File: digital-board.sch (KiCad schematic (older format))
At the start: 233 parts, among them IC1 ATMEGA6450-A, J1 CONN_20X2, Q1 2N3904, Q2 2N3904, SW15 TACT_SWITCH, SW16 TACT_SWITCH, SW17 TACT_SWITCH, SW18 TACT_SWITCH, SW19 TACT_SWITCH, SW20 TACT_SWITCH, SW21 TACT_SWITCH, SW22 TACT_SWITCH, SW23 TACT_SWITCH, U1 DG419, U10 74LVC1G32, U11 74HC165, U12 74AC595, U13 74AC595, U14 74HC165, U15 74AC595, U16 74AC595, U2 74HC4067, U3 R-78E5.0-1.0, U4 74HC4067, U5 74LS573, U6 74LS573, U7 74LVC2G04, U8 74AC595, U9 74HC165, X1 MIDI OUT, X2 MIDI IN, X3 MIDI THRU

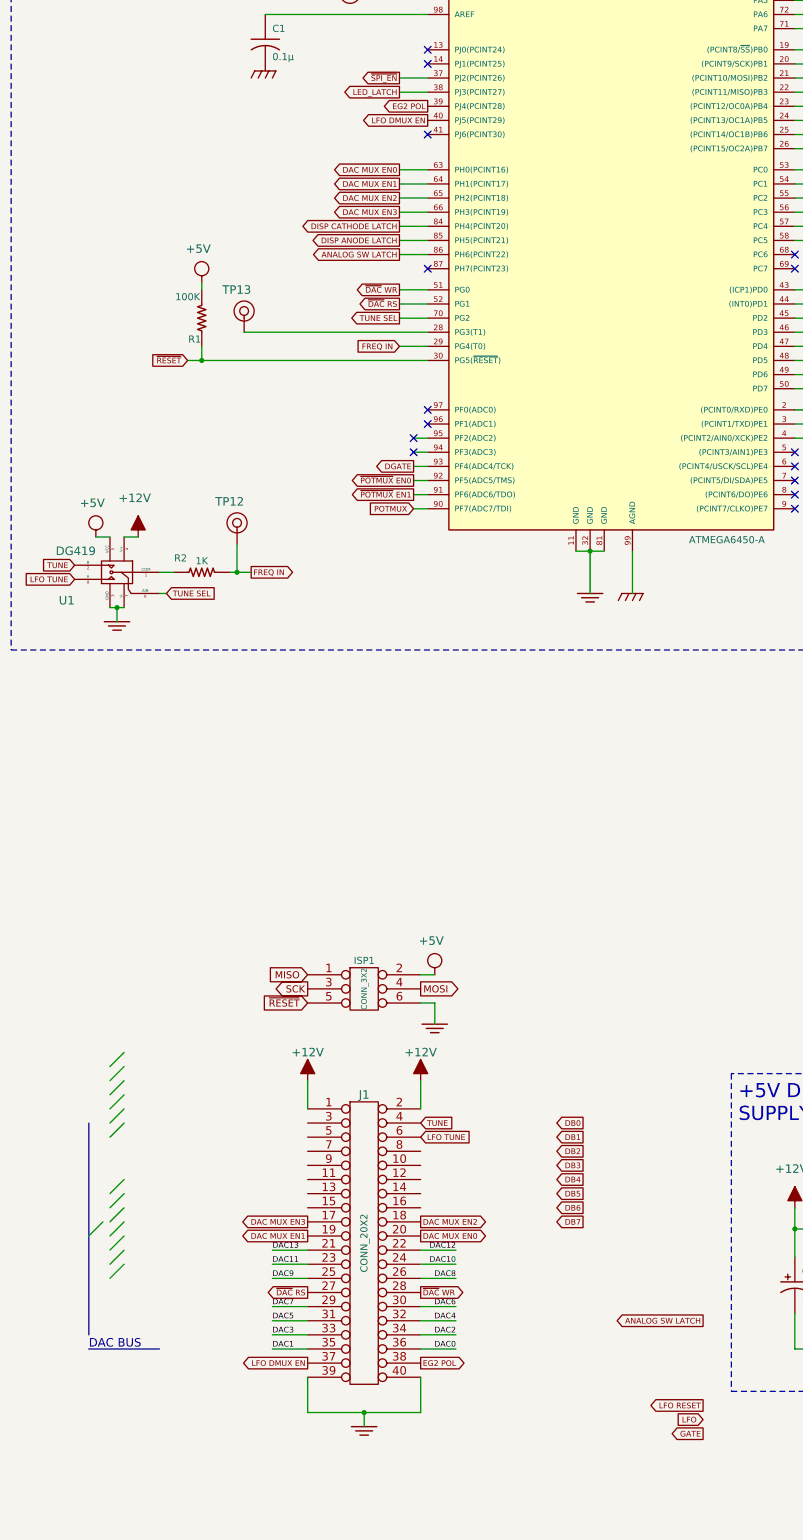
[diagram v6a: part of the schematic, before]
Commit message: almost done routing DAC and DATABUS to J1
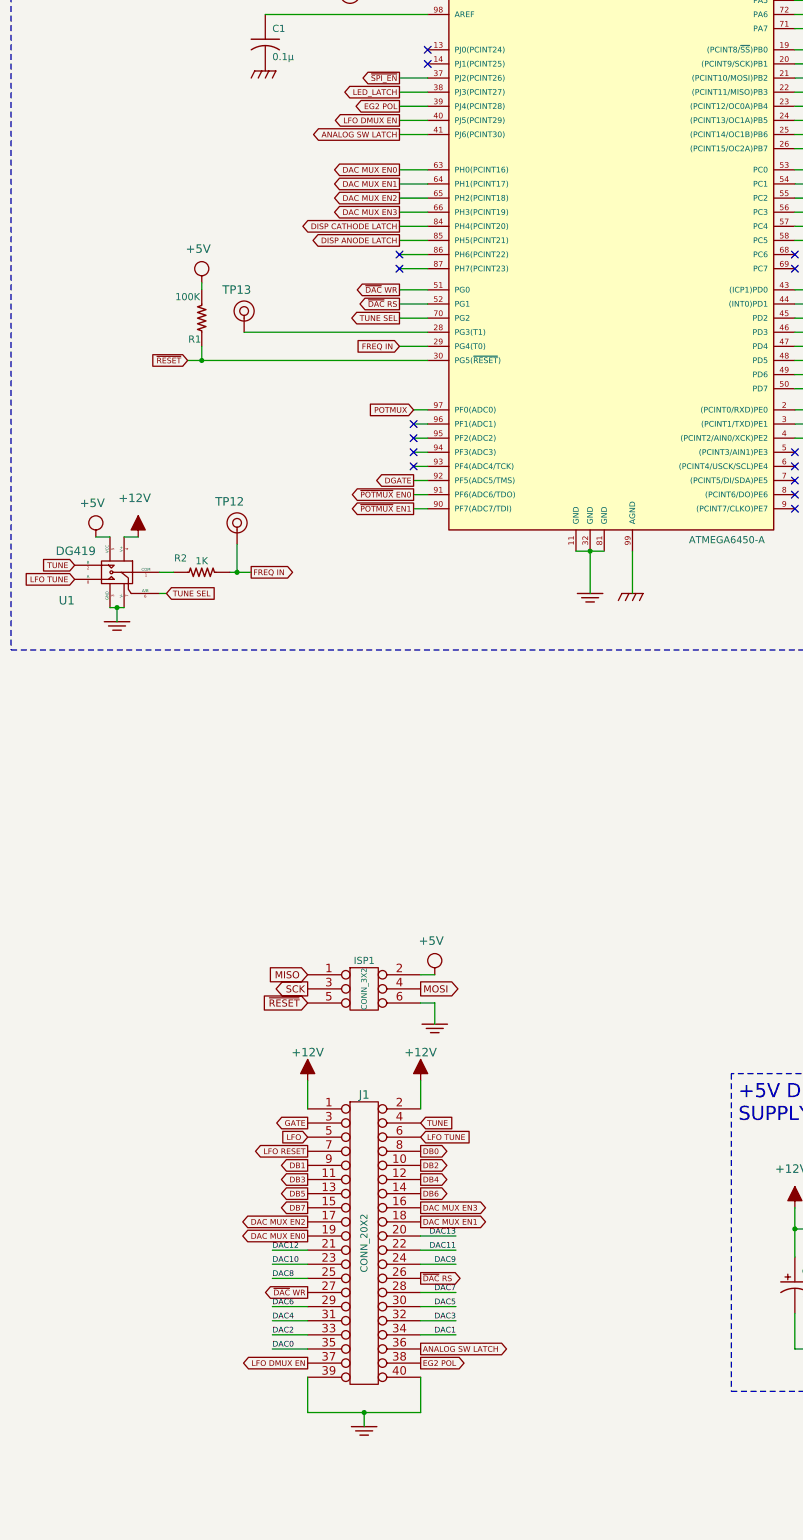
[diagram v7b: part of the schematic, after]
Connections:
- wire segments 935 -> 941
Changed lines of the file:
@@
 Text GLabel 3350 4650 0    40   Output ~ 0
 ~DAC WR
-Text GLabel 3450 6200 0    40   Input ~ 0
+Text GLabel 3450 5500 0    40   Input ~ 0
 POTMUX
 $Comp
@@
 Text GLabel 3200 18800 0    40   Input ~ 0
 ~POTMUX EN0
-Text GLabel 3450 6100 0    40   Output ~ 0
+Text GLabel 3450 6200 0    40   Output ~ 0
 ~POTMUX EN1
 Text GLabel 3350 4300 0    40   Output ~ 0
@@
 Text GLabel 3350 4200 0    40   Output ~ 0
 DISP CATHODE LATCH
-Text GLabel 3450 6000 0    40   Output ~ 0
+Text GLabel 3450 6100 0    40   Output ~ 0
 ~POTMUX EN0
 $Comp
@@
 	0    -1   -1   0
 $EndComp
-Text GLabel 4650 10550 0    40   Output ~ 0
+Text GLabel 3500 10750 2    40   Output ~ 0
 DB0
-Text GLabel 4650 10650 0    40   Output ~ 0
+Text GLabel 2700 10850 0    40   Output ~ 0
 DB1
-Text GLabel 4650 10750 0    40   Output ~ 0
+Text GLabel 3500 10850 2    40   Output ~ 0
 DB2
-Text GLabel 4650 10850 0    40   Output ~ 0
+Text GLabel 2700 10950 0    40   Output ~ 0
 DB3
-Text GLabel 4650 10950 0    40   Output ~ 0
+Text GLabel 3500 10950 2    40   Output ~ 0
 DB4
-Text GLabel 4650 11050 0    40   Output ~ 0
+Text GLabel 2700 11050 0    40   Output ~ 0
 DB5
-Text GLabel 4650 11150 0    40   Output ~ 0
+Text GLabel 3500 11050 2    40   Output ~ 0
 DB6
-Text GLabel 4650 11250 0    40   Output ~ 0
+Text GLabel 2700 11150 0    40   Output ~ 0
 DB7
-Text GLabel 5500 11950 0    40   Output ~ 0
+Text GLabel 3500 12150 2    40   Output ~ 0
 ANALOG SW LATCH
 Text GLabel 3500 10650 2    40   Input ~ 0
 LFO TUNE
-Text GLabel 5500 12750 0    40   Output ~ 0
+Text GLabel 2700 10550 0    40   Output ~ 0
 GATE
-Text GLabel 3500 11350 2    40   Output ~ 0
-DAC MUX EN0
 Text GLabel 2700 11350 0    40   Output ~ 0
-DAC MUX EN1
+DAC MUX EN0
 Text GLabel 3500 11250 2    40   Output ~ 0
-DAC MUX EN2
+DAC MUX EN1
 Text GLabel 2700 11250 0    40   Output ~ 0
+DAC MUX EN2
+Text GLabel 3500 11150 2    40   Output ~ 0
 DAC MUX EN3
 Text GLabel 3500 10550 2    40   Input ~ 0
@@
 Text GLabel 2700 12250 0    40   Output ~ 0
 LFO DMUX EN
-Text GLabel 5500 12550 0    40   Output ~ 0
+Text GLabel 2700 10750 0    40   Output ~ 0
 LFO RESET
-Text GLabel 5500 12650 0    40   Input ~ 0
+Text GLabel 2700 10650 0    40   Input ~ 0
 LFO
 $Comp
@@
 Text Notes 700  800  0    100  ~ 0
 MCU
-Text GLabel 3500 11750 2    40   Output ~ 0
-~DAC WR
 Text GLabel 2700 11750 0    40   Output ~ 0
+~DAC WR
+Text GLabel 3500 11650 2    40   Output ~ 0
 ~DAC RS
-Text Label 3750 12150 2    40   ~ 0
-DAC0
 Text Label 2450 12150 0    40   ~ 0
-DAC1
+DAC0
 Text Label 3750 12050 2    40   ~ 0
-DAC2
+DAC1
 Text Label 2450 12050 0    40   ~ 0
-DAC3
+DAC2
 Text Label 3750 11950 2    40   ~ 0
-DAC4
+DAC3
 Text Label 2450 11950 0    40   ~ 0
-DAC5
+DAC4
 Text Label 3750 11850 2    40   ~ 0
-DAC6
+DAC5
 Text Label 2450 11850 0    40   ~ 0
+DAC6
+Text Label 3750 11750 2    40   ~ 0
 DAC7
-Text Label 3750 11650 2    40   ~ 0
-DAC8
 Text Label 2450 11650 0    40   ~ 0
-DAC9
+DAC8
 Text Label 3750 11550 2    40   ~ 0
-DAC10
+DAC9
 Text Label 2450 11550 0    40   ~ 0
-DAC11
+DAC10
 Text Label 3750 11450 2    40   ~ 0
-DAC12
+DAC11
 Text Label 2450 11450 0    40   ~ 0
+DAC12
+Text Label 3750 11350 2    40   ~ 0
 DAC13
-Entry Wire Line
-	1400 10150 1300 10250
-Entry Wire Line
-	1400 10050 1300 10150
-Entry Wire Line
-	1400 11550 1300 11650
-Entry Wire Line
-	1400 11450 1300 11550
-Entry Wire Line
-	1400 11350 1300 11450
-Entry Wire Line
-	1400 11250 1300 11350
-Entry Wire Line
-	1400 11150 1300 11250
-Entry Wire Line
-	1400 11050 1300 11150
-Entry Wire Line
-	1400 10950 1300 11050
-Entry Wire Line
-	1250 11250 1150 11350
-Entry Wire Line
-	1400 10550 1300 10650
-Entry Wire Line
-	1400 10450 1300 10550
-Entry Wire Line
-	1400 10350 1300 10450
-Entry Wire Line
-	1400 10250 1300 10350
-Text Notes 1150 12150 0    60   ~ 0
-DAC BUS
 $Comp
 L GND_E #PWR035
@@
 Text GLabel 3350 4750 0    40   Output ~ 0
 ~DAC RS
-Text GLabel 3350 4400 0    40   Output ~ 0
+Text GLabel 3350 3550 0    40   Output ~ 0
 ANALOG SW LATCH
 Text GLabel 3350 3800 0    40   Output ~ 0
@@
 Text GLabel 3350 4100 0    40   Output ~ 0
 DAC MUX EN3
-Text GLabel 3550 3450 0    40   Output ~ 0
+Text GLabel 3350 3450 0    40   Output ~ 0
 LFO DMUX EN
-Text GLabel 3450 5900 0    40   Output ~ 0
+Text GLabel 3450 6000 0    40   Output ~ 0
 DGATE
 Text GLabel 3500 12250 2    40   Output ~ 0
 EG2 POL
-Text GLabel 3550 3350 0    40   Output ~ 0
+Text GLabel 3350 3350 0    40   Output ~ 0
 EG2 POL
 $Comp
@@
 	1    0    0    -1
 $EndComp
-NoConn ~ 3550 5500
-NoConn ~ 3550 5600
+NoConn ~ 3450 5900
+NoConn ~ 3450 5600
 $Comp
 L CONN_1 TP13
@@
 	1    0    0    -1
 $EndComp
-NoConn ~ 3550 4500
+NoConn ~ 3350 4500
 $Comp
 L CONN_1 TP12
@@
 Wire Wire Line
 	6750 11600 6750 12250
-Wire Bus Line
-	1650 12150 1150 12150
-Wire Bus Line
-	1150 10550 1150 12050
+Wire Wire Line
+	3500 11350 3750 11350
 Wire Wire Line
 	2700 11450 2450 11450
@@
 	2700 11650 2450 11650
 Wire Wire Line
-	3500 11650 3750 11650
+	3500 11750 3750 11750
 Wire Wire Line
 	2700 11850 2450 11850
@@
 	3500 11950 3750 11950
 Wire Wire Line
-	2700 12050 2450 12050
+	2450 12050 2700 12050
 Wire Wire Line
 	3750 12050 3500 12050
 Wire Wire Line
 	2450 12150 2700 12150
-Wire Wire Line
-	3750 12150 3500 12150
 Wire Notes Line
 	8750 600  600  600
@@
 NoConn ~ 3550 2950
 NoConn ~ 3550 3050
-NoConn ~ 3550 3550
+NoConn ~ 3350 4400
 NoConn ~ 3450 5700
 NoConn ~ 3450 5800
@@
 Wire Wire Line
 	3550 3150 3350 3150
+Wire Wire Line
+	3350 4500 3550 4500
+Wire Wire Line
+	3350 3350 3550 3350
+Wire Wire Line
+	3350 3450 3550 3450
+Wire Wire Line
+	3350 3550 3550 3550
+Wire Wire Line
+	3450 5500 3550 5500
+Wire Wire Line
+	3550 5600 3450 5600
 $EndSCHEMATC

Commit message: changed TL1240 component and module pin numbering
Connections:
- wire segments 941 -> 829
